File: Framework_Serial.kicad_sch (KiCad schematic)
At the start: 20 parts, among them J1 Conn_01x07_Male, P1 USB_C_Plug_USB2.0, U1 USBLC6-2SC6, U2 CP2102N-A01-GQFN28

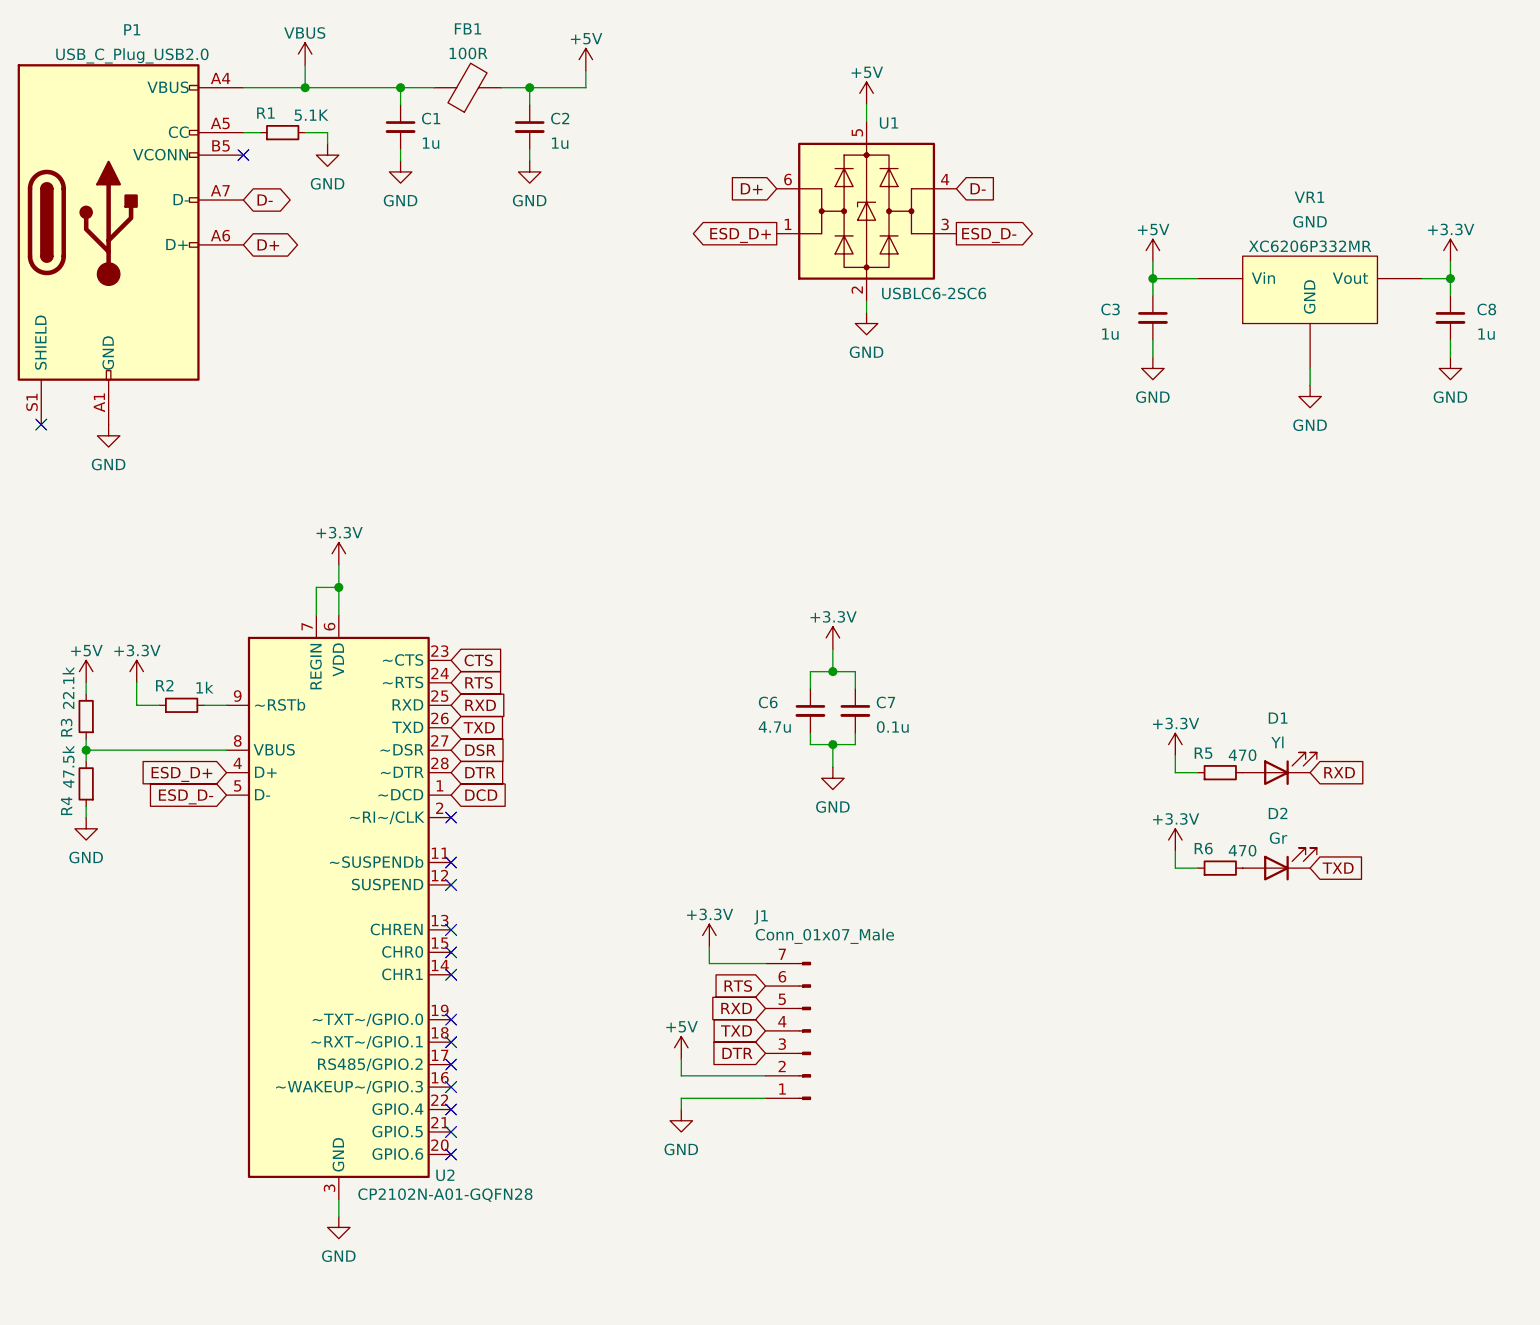
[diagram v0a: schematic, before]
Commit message: added testpoints, changed to AMS1117-3.3
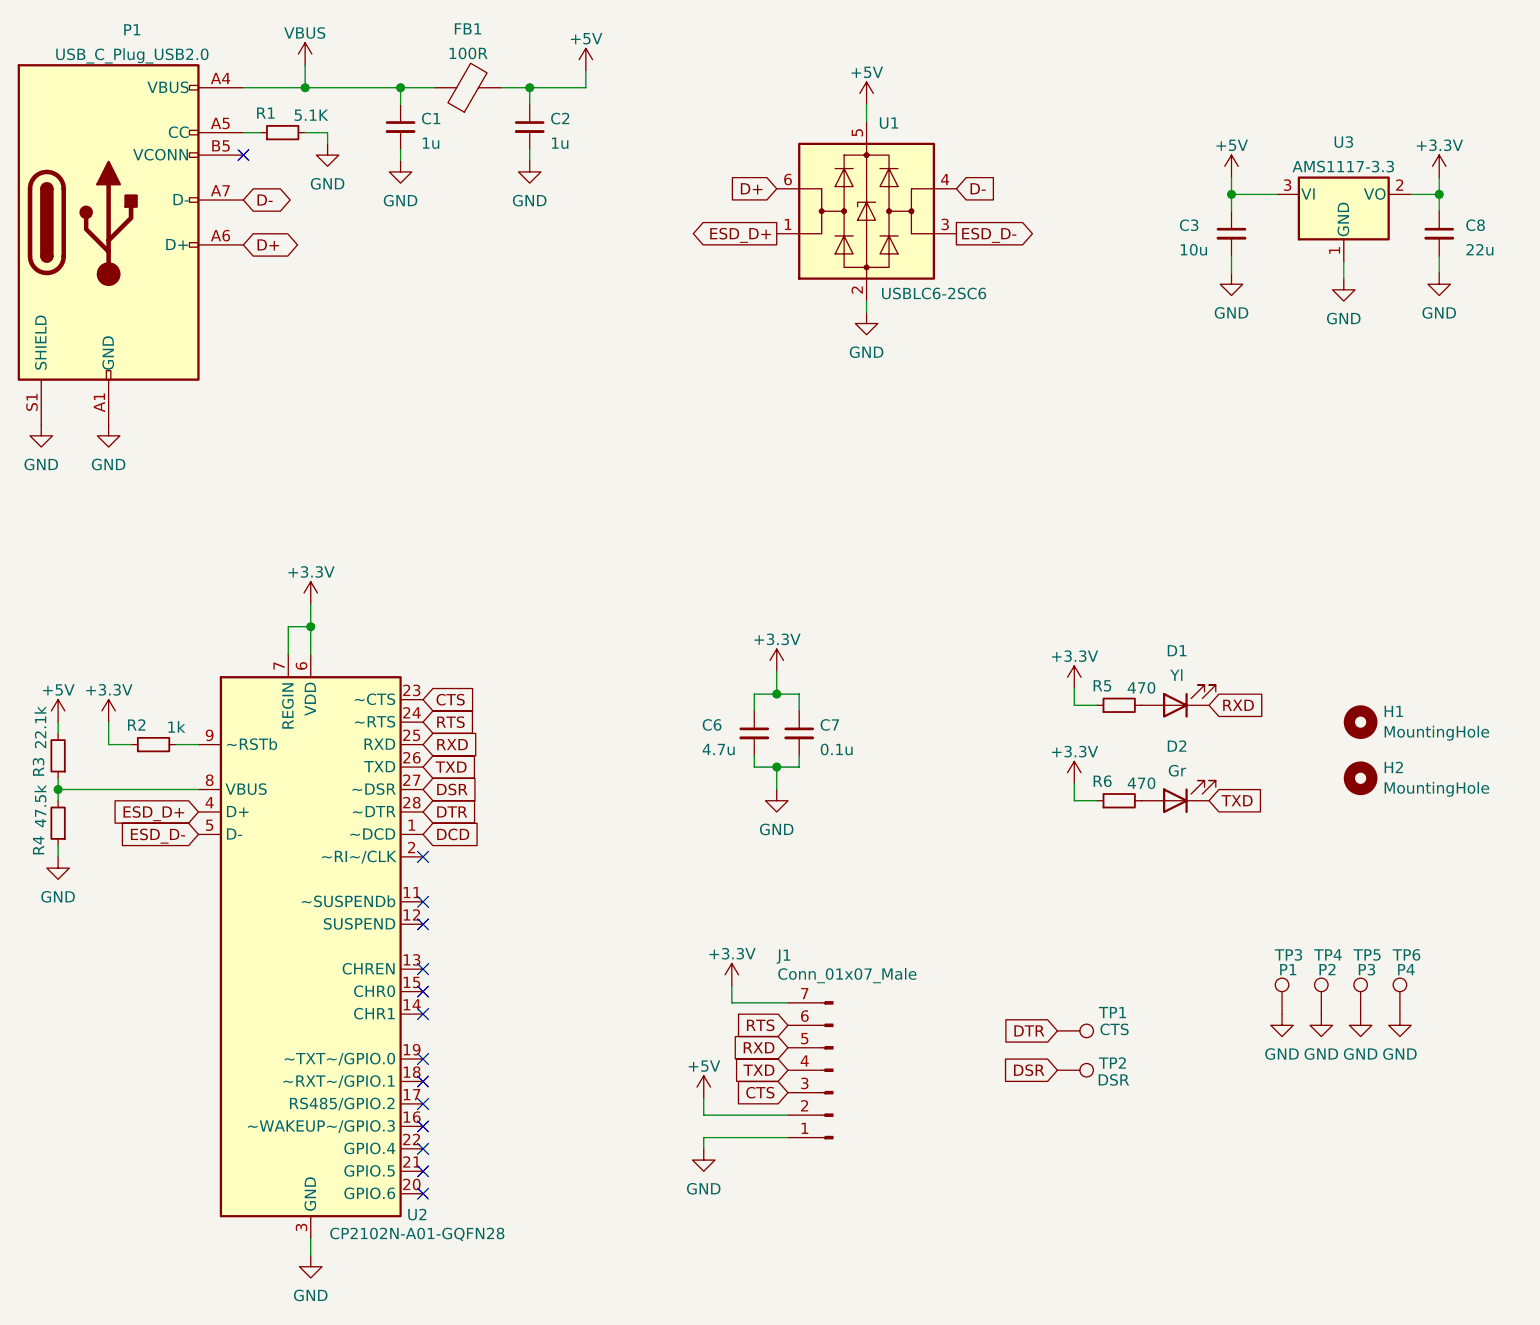
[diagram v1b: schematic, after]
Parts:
- removed VR1: SOT-23_XC6206P332MR, Package_TO_SOT_SMD:SOT-89-3, symbol lc_LDO:SOT-23_XC6206P332MR
- added H1, H2: MountingHole, MountingHole:MountingHole_2.2mm_M2, symbol Mechanical:MountingHole
- added TP1: CTS, TestPoint:TestPoint_Pad_D1.0mm, symbol Connector:TestPoint
- added TP2: DSR, TestPoint:TestPoint_Pad_D1.0mm, symbol Connector:TestPoint
- added TP3: P1, TestPoint:TestPoint_Pad_1.5x1.5mm, symbol Connector:TestPoint
- added TP4: P2, TestPoint:TestPoint_Pad_1.5x1.5mm, symbol Connector:TestPoint
- added TP5: P3, TestPoint:TestPoint_Pad_1.5x1.5mm, symbol Connector:TestPoint
- added TP6: P4, TestPoint:TestPoint_Pad_1.5x1.5mm, symbol Connector:TestPoint
- added U3: AMS1117-3.3, Package_TO_SOT_SMD:SOT-223-3_TabPin2, symbol Regulator_Linear:AMS1117-3.3
- C1, C2: LCSC Part # (none) -> C15849
- C3: value 1u -> 10u; footprint Capacitor_SMD:C_0805_2012Metric -> Capacitor_SMD:C_0603_1608Metric; LCSC Part # (none) -> C19702
- C6: footprint Capacitor_SMD:C_0805_2012Metric -> Capacitor_SMD:C_0603_1608Metric; LCSC Part # (none) -> C19666
- C7: footprint Capacitor_SMD:C_0603_1608Metric -> Capacitor_SMD:C_0402_1005Metric; LCSC Part # (none) -> C1525
- C8: value 1u -> 22u; LCSC Part # (none) -> C45783
- D1: LCSC Part # (none) -> C72038
- D2: LCSC Part # (none) -> C72043
- FB1: LCSC Part # (none) -> C1015
- R1: footprint Resistor_SMD:R_0805_2012Metric -> Resistor_SMD:R_0402_1005Metric; LCSC Part # (none) -> C25905
- R2: footprint Resistor_SMD:R_0805_2012Metric -> Resistor_SMD:R_0402_1005Metric; LCSC Part # (none) -> C11702
- R3: footprint Resistor_SMD:R_0805_2012Metric -> Resistor_SMD:R_0402_1005Metric; LCSC Part # (none) -> C25768
- R4: footprint Resistor_SMD:R_0805_2012Metric -> Resistor_SMD:R_0402_1005Metric; LCSC Part # (none) -> C25792
- R5, R6: LCSC Part # (none) -> C17710
- U1: LCSC Part # (none) -> C7519
- U2: LCSC Part # (none) -> C6568
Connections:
- net +3V3: now also U3.2 (VO)
- net +5V: now also U3.3 (VI)
- net CTS: now also J1.3 (Pin_3)
- net DSR: now also TP2.1
- net DTR: now also TP1.1; no longer J1.3 (Pin_3)
- net GND: now also P1.S1 (SHIELD), TP3.1, TP4.1, TP5.1, TP6.1, U3.1 (GND)
- no-connect marks 15 -> 14
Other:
- moved on the sheet: C3, C6, C7, C8, D1, D2, J1, R2, R3, R4, R5, R6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

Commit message: changed LCSC parts number for LED resistor
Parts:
- R5, R6: LCSC Part # C17710 -> C23179
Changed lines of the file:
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@@
       (effects (font (size 1.27 1.27)) hide)
     )
-    (property "LCSC Part #" "C17710" (id 4) (at 142.875 92.71 0)
+    (property "LCSC Part #" "C23179" (id 4) (at 142.875 92.71 0)
       (effects (font (size 1.27 1.27)) hide)
     )
@@
       (effects (font (size 1.27 1.27)) hide)
     )
-    (property "LCSC Part #" "C17710" (id 4) (at 142.875 103.505 0)
+    (property "LCSC Part #" "C23179" (id 4) (at 142.875 103.505 0)
       (effects (font (size 1.27 1.27)) hide)
     )
